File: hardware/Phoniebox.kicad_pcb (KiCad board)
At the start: 2 copper layers, 65 x 56.5 mm, 84 parts, among them J1 GPIO, J2 Screw_Terminal_01x08, J3 Screw_Terminal_01x08, J4 Screw_Terminal_01x08, J5 Conn_01x04_Male, J6 Conn_01x08_Male, J7 USB_C_Receptacle_USB2.0, Q1 2N7002, Q2 2N7002, Q3 2N7002, Q4 2N7002, Q5 2N7002, Q6 2N7002, Q7 AO3401A, Q8 2N7002, U1 PAM8406, U2 TPS79333-EP, U3 PCM5102, U4 CAT24C32

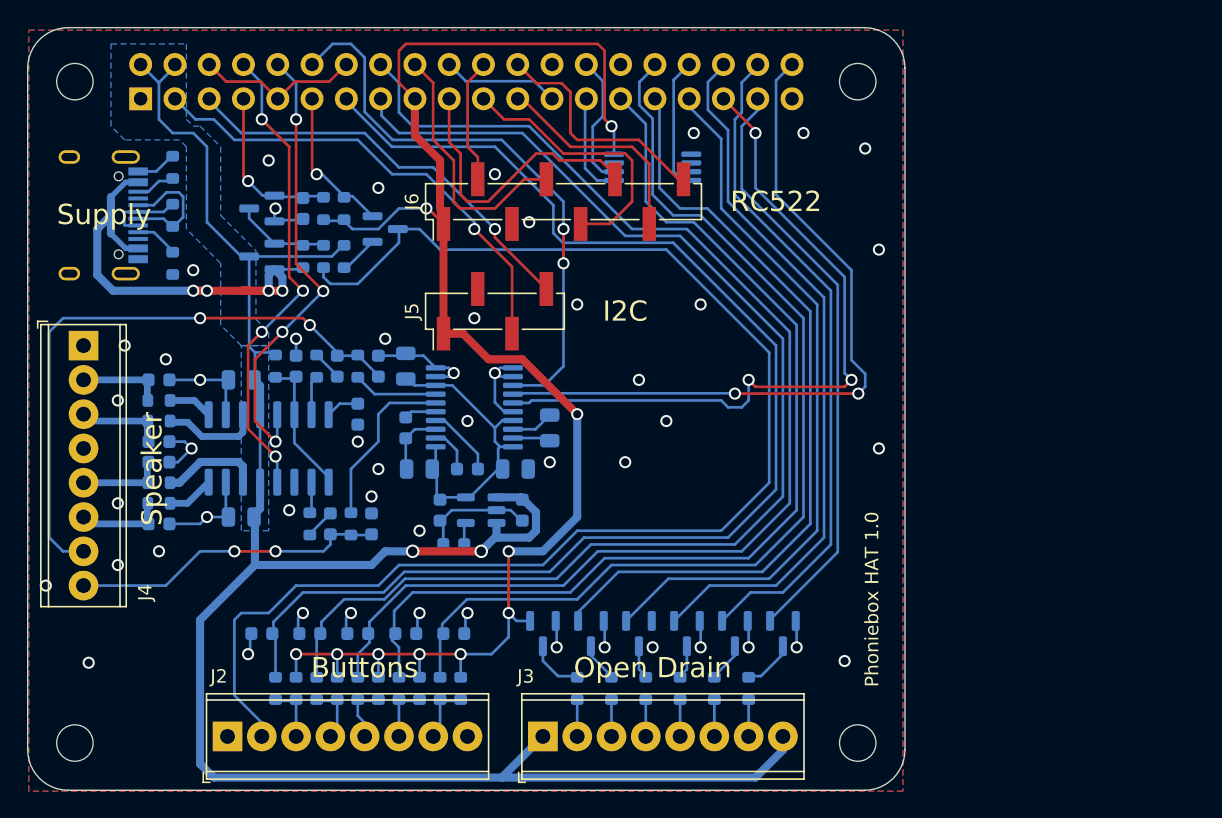
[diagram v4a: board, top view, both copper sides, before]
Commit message: Add USB-C 3D model. Add pinning info in silkscreen for all connectors.
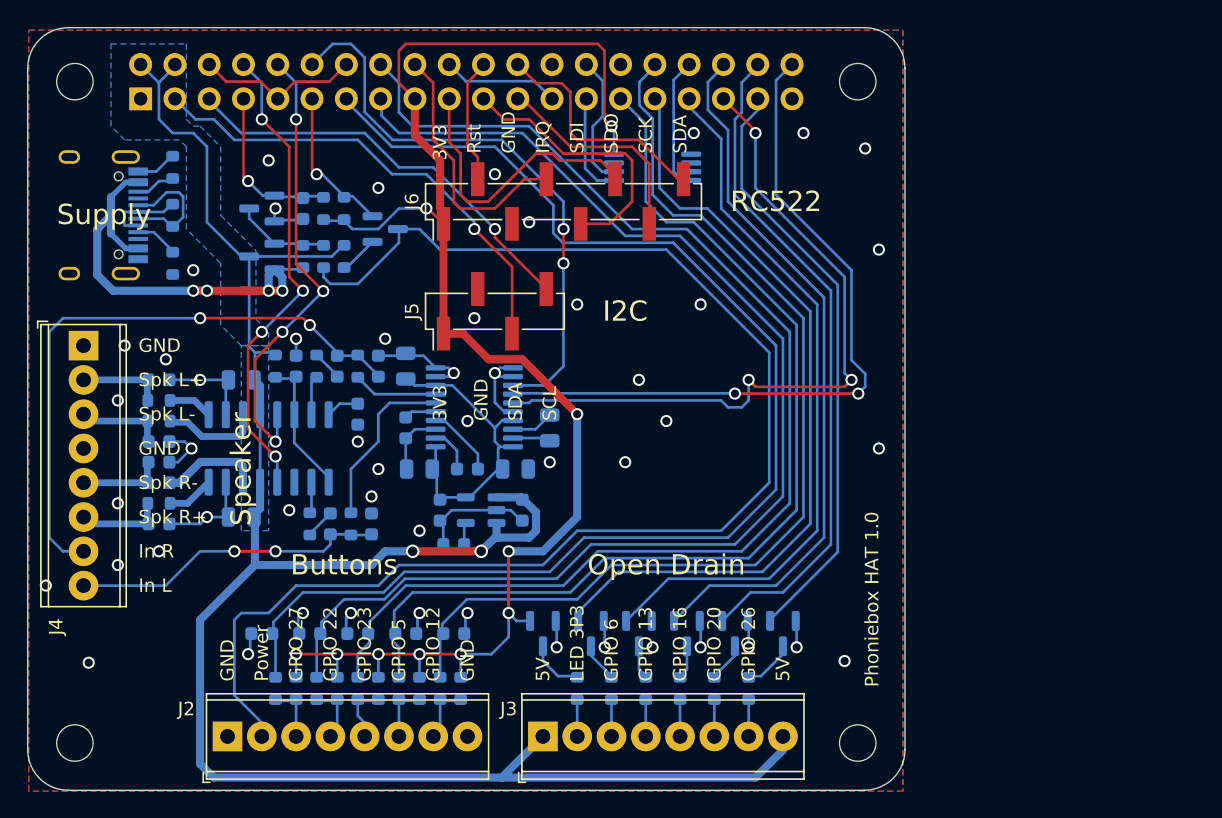
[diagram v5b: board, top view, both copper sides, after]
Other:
- board text added: "3V3"
- board text added: "5V"
- board text added: "GND"
- board text added: "GPIO 12"
- board text added: "GPIO 13"
- board text added: "GPIO 16"
- board text added: "GPIO 20"
- board text added: "GPIO 22"
- board text added: "GPIO 23"
- board text added: "GPIO 26"
- board text added: "GPIO 27"
- board text added: "GPIO 5"
- board text added: "GPIO 6"
- board text added: "IRQ"
- board text added: "In L"
- board text added: "In R"
- board text added: "LED 3P3"
- board text added: "Power"
- board text added: "Rst"
- board text added: "SCK"
- board text added: "SCL"
- board text added: "SDA"
- board text added: "SDI"
- board text added: "SDO"
- board text added: "Spk L+"
- board text added: "Spk L-"
- board text added: "Spk R+"
- board text added: "Spk R-"
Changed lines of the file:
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@@
     (property "Sheetname" "")
     (attr through_hole)
-    (fp_text reference "J4" (at 18.288 -4.572 90) (layer "F.SilkS")
+    (fp_text reference "J4" (at 20.828 2.032 90) (layer "F.SilkS")
       (effects (font (size 1 1) (thickness 0.15)))
     )
@@
     (property "Sheetname" "")
     (attr through_hole)
-    (fp_text reference "J2" (at -0.635 -4.445) (layer "F.SilkS")
+    (fp_text reference "J2" (at -3.048 -2.032) (layer "F.SilkS")
       (effects (font (size 1 1) (thickness 0.15)))
     )
@@
     (property "Sheetname" "")
     (attr through_hole)
-    (fp_text reference "J3" (at -1.27 -4.445) (layer "F.SilkS")
+    (fp_text reference "J3" (at -2.54 -2.032) (layer "F.SilkS")
       (effects (font (size 1 1) (thickness 0.15)))
     )
@@
     (property "Sheetname" "")
     (attr smd)
-    (fp_text reference "U4" (at 5.588 1.016) (layer "B.SilkS")
+    (fp_text reference "U4" (at -3.048 -2.54) (layer "B.SilkS")
       (effects (font (size 1 1) (thickness 0.15)) (justify mirror))
     )
@@
     (property "Sheetname" "Buttons")
     (attr smd)
-    (fp_text reference "C14" (at 0 3.048) (layer "B.SilkS")
+    (fp_text reference "C14" (at 1.524 1.524) (layer "B.SilkS")
       (effects (font (size 1 1) (thickness 0.15)) (justify mirror))
     )
@@
     (property "Sheetname" "Buttons")
     (attr smd)
-    (fp_text reference "C9" (at 0 3.048) (layer "B.SilkS")
+    (fp_text reference "C9" (at 2.032 1.524) (layer "B.SilkS")
       (effects (font (size 1 1) (thickness 0.15)) (justify mirror))
     )
@@
     (property "Sheetname" "Buttons")
     (attr smd)
-    (fp_text reference "C15" (at -0.14058 -3.048 180) (layer "B.SilkS")
+    (fp_text reference "C15" (at -1.016 -1.524 180) (layer "B.SilkS")
       (effects (font (size 1 1) (thickness 0.15)) (justify mirror))
     )
@@
       (rotate (xyz 0 0 0))
     )
+    (model "${KIPRJMOD}/TYPE-C-31-M-12.stp"
+      (offset (xyz -4.47 -3.7 0))
+      (scale (xyz 1 1 1))
+      (rotate (xyz 90 180 180))
+    )
   )
   (footprint "Resistor_SMD:R_0603_1608Metric" (layer "B.Cu")
@@
     (property "Sheetname" "Buttons")
     (attr smd)
-    (fp_text reference "R7" (at 0.508 2.032 90) (layer "B.SilkS")
+    (fp_text reference "R7" (at 0 1.524 90) (layer "B.SilkS")
       (effects (font (size 1 1) (thickness 0.15)) (justify mirror))
     )
@@
     (property "Sheetname" "Buttons")
     (attr smd)
-    (fp_text reference "C8" (at 0 3.048) (layer "B.SilkS")
+    (fp_text reference "C8" (at 1.524 1.524) (layer "B.SilkS")
       (effects (font (size 1 1) (thickness 0.15)) (justify mirror))
     )
@@
     (property "Sheetname" "Buttons")
     (attr smd)
-    (fp_text reference "C16" (at -0.14058 -3.048 180) (layer "B.SilkS")
+    (fp_text reference "C16" (at -0.508 -1.524 180) (layer "B.SilkS")
       (effects (font (size 1 1) (thickness 0.15)) (justify mirror))
     )
@@
     (property "Sheetname" "OnOffSHIM")
     (attr smd)
-    (fp_text reference "D1" (at 2.54 0.508 90) (layer "B.SilkS")
+    (fp_text reference "D1" (at 3.048 1.016) (layer "B.SilkS")
       (effects (font (size 1 1) (thickness 0.15)) (justify mirror))
     )
@@
     (property "Sheetname" "Audio")
     (attr smd)
-    (fp_text reference "C7" (at -1.016 -2.032) (layer "B.SilkS")
+    (fp_text reference "C7" (at 0 -2.032) (layer "B.SilkS")
       (effects (font (size 1 1) (thickness 0.15)) (justify mirror))
     )
@@
   (gr_arc (start 162 43.5) (mid 164.12132 44.37868) (end 165 46.5) (layer "Edge.Cuts") (width 0.1))
   (gr_line locked (start 103 100) (end 162 100) (layer "Edge.Cuts") (width 0.1))
-  (gr_text "Speaker" (at 109.22 76.2 90) (layer "F.SilkS")
+  (gr_text "GND" (at 133.604 72.644 90) (layer "F.SilkS")
+    (effects (font (size 1 1) (thickness 0.15)) (justify left))
+  )
+  (gr_text "Speaker" (at 115.824 76.2 90) (layer "F.SilkS")
     (effects (font (size 1.5 1.5) (thickness 0.3)))
   )
+  (gr_text "GPIO 27" (at 119.888 91.948 90) (layer "F.SilkS")
+    (effects (font (size 1 1) (thickness 0.15)) (justify left))
+  )
+  (gr_text "GPIO 22" (at 122.428 91.948 90) (layer "F.SilkS")
+    (effects (font (size 1 1) (thickness 0.15)) (justify left))
+  )
+  (gr_text "IRQ" (at 138.176 52.832 90) (layer "F.SilkS")
+    (effects (font (size 1 1) (thickness 0.15)) (justify left))
+  )
+  (gr_text "Spk R-" (at 108.204 77.216) (layer "F.SilkS")
+    (effects (font (size 1 1) (thickness 0.15)) (justify left))
+  )
+  (gr_text "3V3" (at 130.556 53.34 90) (layer "F.SilkS")
+    (effects (font (size 1 1) (thickness 0.15)) (justify left))
+  )
+  (gr_text "LED 3P3" (at 140.716 91.948 90) (layer "F.SilkS")
+    (effects (font (size 1 1) (thickness 0.15)) (justify left))
+  )
+  (gr_text "SDO" (at 143.256 52.832 90) (layer "F.SilkS")
+    (effects (font (size 1 1) (thickness 0.15)) (justify left))
+  )
+  (gr_text "GND" (at 108.204 67.056) (layer "F.SilkS")
+    (effects (font (size 1 1) (thickness 0.15)) (justify left))
+  )
+  (gr_text "GPIO 5" (at 127.508 91.948 90) (layer "F.SilkS")
+    (effects (font (size 1 1) (thickness 0.15)) (justify left))
+  )
+  (gr_text "GND" (at 132.588 91.948 90) (layer "F.SilkS")
+    (effects (font (size 1 1) (thickness 0.15)) (justify left))
+  )
+  (gr_text "Spk L+" (at 108.204 69.596) (layer "F.SilkS")
+    (effects (font (size 1 1) (thickness 0.15)) (justify left))
+  )
   (gr_text "I2C" (at 144.272 64.516) (layer "F.SilkS")
     (effects (font (size 1.5 1.5) (thickness 0.3)))
   )
+  (gr_text "Power" (at 117.348 91.948 90) (layer "F.SilkS")
+    (effects (font (size 1 1) (thickness 0.15)) (justify left))
+  )
+  (gr_text "3V3" (at 130.556 72.644 90) (layer "F.SilkS")
+    (effects (font (size 1 1) (thickness 0.15)) (justify left))
+  )
+  (gr_text "Spk L-" (at 108.204 72.136) (layer "F.SilkS")
+    (effects (font (size 1 1) (thickness 0.15)) (justify left))
+  )
+  (gr_text "GPIO 6" (at 143.256 91.948 90) (layer "F.SilkS")
+    (effects (font (size 1 1) (thickness 0.15)) (justify left))
+  )
+  (gr_text "GND" (at 135.636 52.832 90) (layer "F.SilkS")
+    (effects (font (size 1 1) (thickness 0.15)) (justify left))
+  )
   (gr_text "Supply" (at 105.664 57.357678) (layer "F.SilkS")
     (effects (font (size 1.5 1.5) (thickness 0.3)))
   )
+  (gr_text "Spk R+" (at 108.204 79.756) (layer "F.SilkS")
+    (effects (font (size 1 1) (thickness 0.15)) (justify left))
+  )
   (gr_text "RC522" (at 155.448 56.388) (layer "F.SilkS")
     (effects (font (size 1.5 1.5) (thickness 0.3)))
   )
-  (gr_text "Buttons" (at 124.968 90.932) (layer "F.SilkS")
+  (gr_text "In L" (at 108.204 84.836) (layer "F.SilkS")
+    (effects (font (size 1 1) (thickness 0.15)) (justify left))
+  )
+  (gr_text "GPIO 23" (at 124.968 91.948 90) (layer "F.SilkS")
+    (effects (font (size 1 1) (thickness 0.15)) (justify left))
+  )
+  (gr_text "SDI" (at 140.716 52.832 90) (layer "F.SilkS")
+    (effects (font (size 1 1) (thickness 0.15)) (justify left))
+  )
+  (gr_text "In R" (at 108.204 82.296) (layer "F.SilkS")
+    (effects (font (size 1 1) (thickness 0.15)) (justify left))
+  )
+  (gr_text "Buttons" (at 123.444 83.312) (layer "F.SilkS")
     (effects (font (size 1.5 1.5) (thickness 0.3)))
   )
+  (gr_text "GND" (at 108.204 74.676) (layer "F.SilkS")
+    (effects (font (size 1 1) (thickness 0.15)) (justify left))
+  )
+  (gr_text "SDA" (at 136.144 72.644 90) (layer "F.SilkS")
+    (effects (font (size 1 1) (thickness 0.15)) (justify left))
+  )
   (gr_text "Phoniebox HAT 1.0" (at 162.56 85.852 90) (layer "F.SilkS")
     (effects (font (size 1 1) (thickness 0.2)))
   )
-  (gr_text "Open Drain" (at 146.304 90.932) (layer "F.SilkS")
+  (gr_text "Open Drain" (at 147.32 83.312) (layer "F.SilkS")
     (effects (font (size 1.5 1.5) (thickness 0.3)))
   )
+  (gr_text "SDA" (at 148.336 52.832 90) (layer "F.SilkS")
+    (effects (font (size 1 1) (thickness 0.15)) (justify left))
+  )
+  (gr_text "GPIO 20" (at 150.876 91.948 90) (layer "F.SilkS")
+    (effects (font (size 1 1) (thickness 0.15)) (justify left))
+  )
+  (gr_text "5V" (at 138.176 91.948 90) (layer "F.SilkS")
+    (effects (font (size 1 1) (thickness 0.15)) (justify left))
+  )
+  (gr_text "GND" (at 114.808 91.948 90) (layer "F.SilkS")
+    (effects (font (size 1 1) (thickness 0.15)) (justify left))
+  )
+  (gr_text "SCL" (at 138.684 72.644 90) (layer "F.SilkS")
+    (effects (font (size 1 1) (thickness 0.15)) (justify left))
+  )
+  (gr_text "GPIO 12" (at 130.048 91.948 90) (layer "F.SilkS")
+    (effects (font (size 1 1) (thickness 0.15)) (justify left))
+  )
+  (gr_text "SCK" (at 145.796 52.832 90) (layer "F.SilkS")
+    (effects (font (size 1 1) (thickness 0.15)) (justify left))
+  )
+  (gr_text "GPIO 13" (at 145.796 91.948 90) (layer "F.SilkS")
+    (effects (font (size 1 1) (thickness 0.15)) (justify left))
+  )
+  (gr_text "GPIO 26" (at 153.416 91.948 90) (layer "F.SilkS")
+    (effects (font (size 1 1) (thickness 0.15)) (justify left))
+  )
+  (gr_text "GPIO 16" (at 148.336 91.948 90) (layer "F.SilkS")
+    (effects (font (size 1 1) (thickness 0.15)) (justify left))
+  )
+  (gr_text "5V" (at 155.956 91.948 90) (layer "F.SilkS")
+    (effects (font (size 1 1) (thickness 0.15)) (justify left))
+  )
+  (gr_text "Rst" (at 133.096 52.832 90) (layer "F.SilkS")
+    (effects (font (size 1 1) (thickness 0.15)) (justify left))
+  )
   (gr_text "USB" (at 177.724 71.552) (layer "Dwgs.User")

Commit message: Fix all ERC warnings. Replace 4u7 capacitor in cut-off circuit by 100 nF cap and 10 kOhm in series to reduce stress on Raspi GPIO.
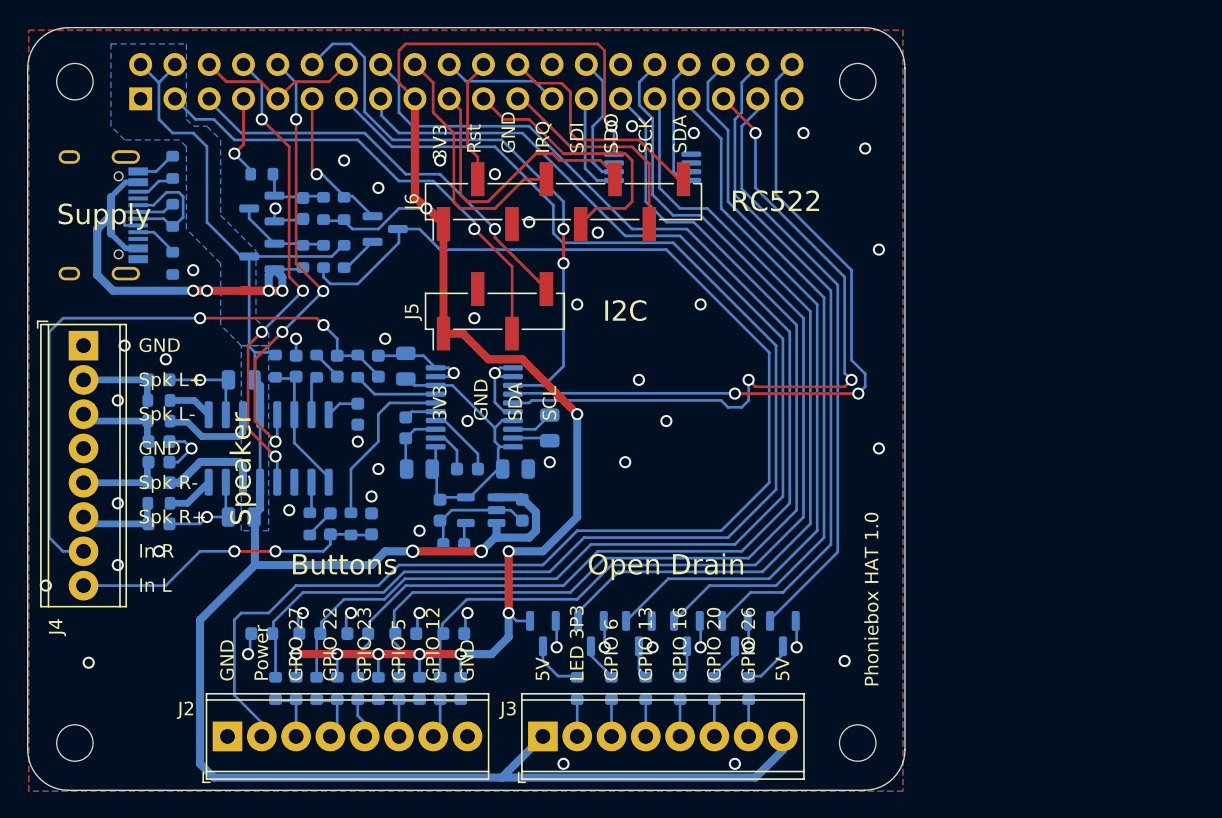
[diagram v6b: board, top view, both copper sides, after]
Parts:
- added R29: 10k, Resistor_SMD:R_0603_1608Metric, B.Cu at (117.3, 54.4)
- C21: value 4u7 -> 100n
- R26: value 1k -> 100k
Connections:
- net +3V3 renamed +3.3V
- net /GPIO17_Trigger renamed /GPIO17_Ctrl_Out
- net /GPIO18 renamed /DAC_BCK
- net /GPIO19 renamed /DAC_LRCK
- net /GPIO21 renamed /DAC_DIN
- net /OnOffSHIM/Q7_G renamed /Supply Cut-Off Circuit/Q7_G
- net /OnOffSHIM/VBUS renamed /Supply Cut-Off Circuit/V_In
- C21 pad 1: /GPIO4_PowerOff -> Net-(C21-Pad1)
- J1 pad 7: /GPIO4_PowerOff -> /GPIO4_PowerKeep
- Q8 pad 1: /GPIO4_PowerOff -> Net-(C21-Pad1)
- R26 pad 1: /GPIO4_PowerOff -> Net-(C21-Pad1)
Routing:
- net /GPIO4_PowerOff: track 12.2 -> 0.00 mm, vias 1 -> 0
- net /GPIO4_PowerKeep: track 0.00 -> 6.37 mm, vias 0 -> 1
- net Net-(C21-Pad1): track 0.00 -> 5.20 mm
- net /INR: track 45.0 -> 45.6 mm
- net GND: vias 51 -> 56

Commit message: Replaced both single row connectors for RC522,I2C by one two row connector. Speaker left and right were mixed in top level schematic -> fixed net names and silkscreen text.
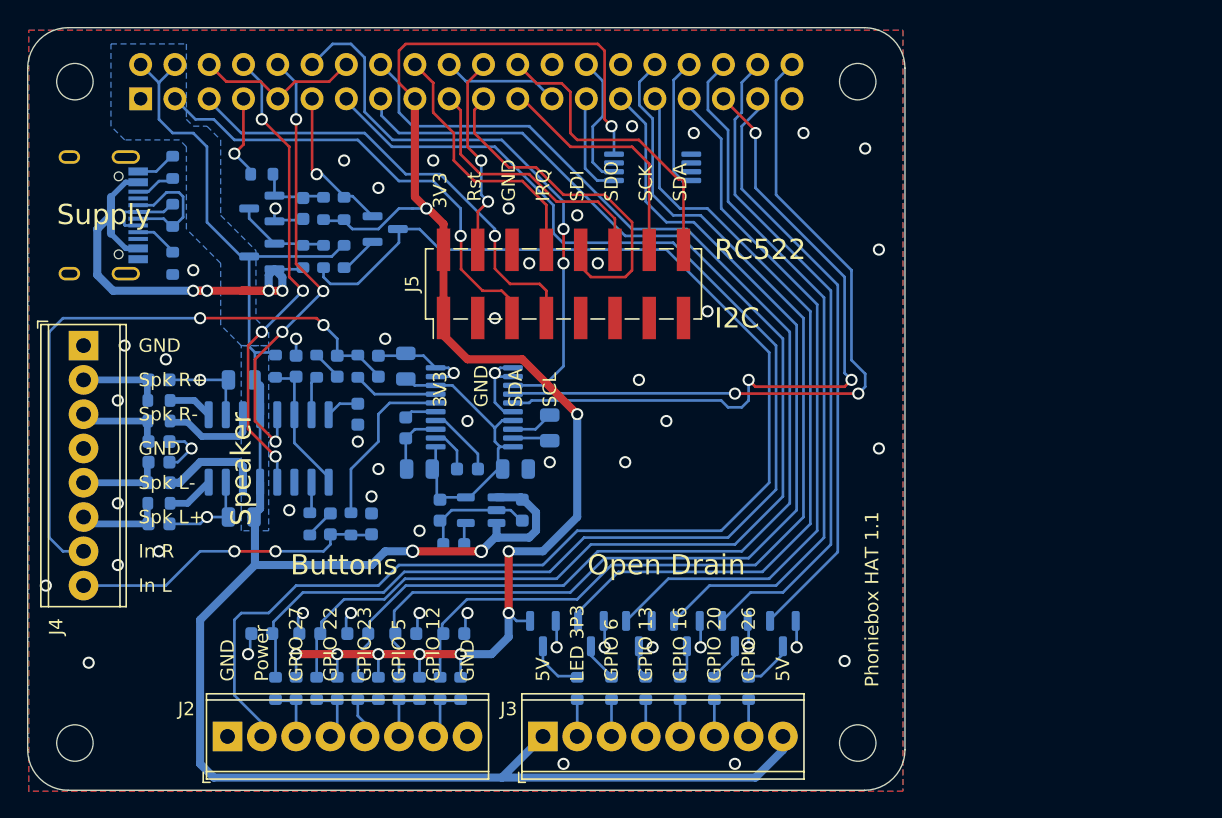
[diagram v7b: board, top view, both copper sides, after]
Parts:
- removed J6: Conn_01x08_Male, Connector_PinHeader_2.54mm:PinHeader_1x08_P2.54mm_Vertical_SMD_Pin1Left
- J5: value Conn_01x04_Male -> Conn_02x08_Odd_Even; footprint Connector_PinHeader_2.54mm:PinHeader_1x04_P2.54mm_Vertical_SMD_Pin1Left -> Connector_PinHeader_2.54mm:PinHeader_2x08_P2.54mm_Vertical_SMD
- R13, R21, R7, R9: value 33k -> 100
- moved J5 5.47 mm to (139.7, 62.5)
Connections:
- C10 pad 1: /SPK_L+ -> /SPK_R+
- C11 pad 1: /SPK_L- -> /SPK_R-
- C12 pad 1: /SPK_R- -> /SPK_L-
- C13 pad 1: /SPK_R+ -> /SPK_L+
- FB1 pad 2: /SPK_L+ -> /SPK_R+
- FB2 pad 2: /SPK_L- -> /SPK_R-
- FB3 pad 2: /SPK_R- -> /SPK_L-
- FB4 pad 2: /SPK_R+ -> /SPK_L+
- J4 pad 2: /SPK_L+ -> /SPK_R+
- J4 pad 3: /SPK_L- -> /SPK_R-
- J4 pad 5: /SPK_R- -> /SPK_L-
- J4 pad 6: /SPK_R+ -> /SPK_L+
- J5 pad 2: GND -> +3.3V
- J5 pad 3: /GPIO2_SDA -> GND
- J5 pad 4: /GPIO3_SCL -> /RST
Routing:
- net /MISO: track 20.3 -> 26.3 mm
- net /RST: track 9.26 -> 15.1 mm, vias 0 -> 2
- net /SDA: track 17.6 -> 22.8 mm
- net /GPIO3_SCL: track 31.2 -> 34.6 mm
- net /SCK: track 16.2 -> 18.1 mm
- net /MOSI: track 21.5 -> 20.2 mm
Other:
- board text added: "Phoniebox HAT 1.1"
- board text removed: "Phoniebox HAT 1.0"
